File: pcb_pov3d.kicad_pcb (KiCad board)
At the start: 4 copper layers, 98 x 90 mm, 95 parts, among them P1 CONN_4X2, P2 CONN_6, P3 MICRO-SD, P4 CONN_2, P5 KNUSB, P6 CONN_12, U1 TLC5955, U2 TLC5955, U3 TLC5955, U4 STM32F40X_LQFP64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

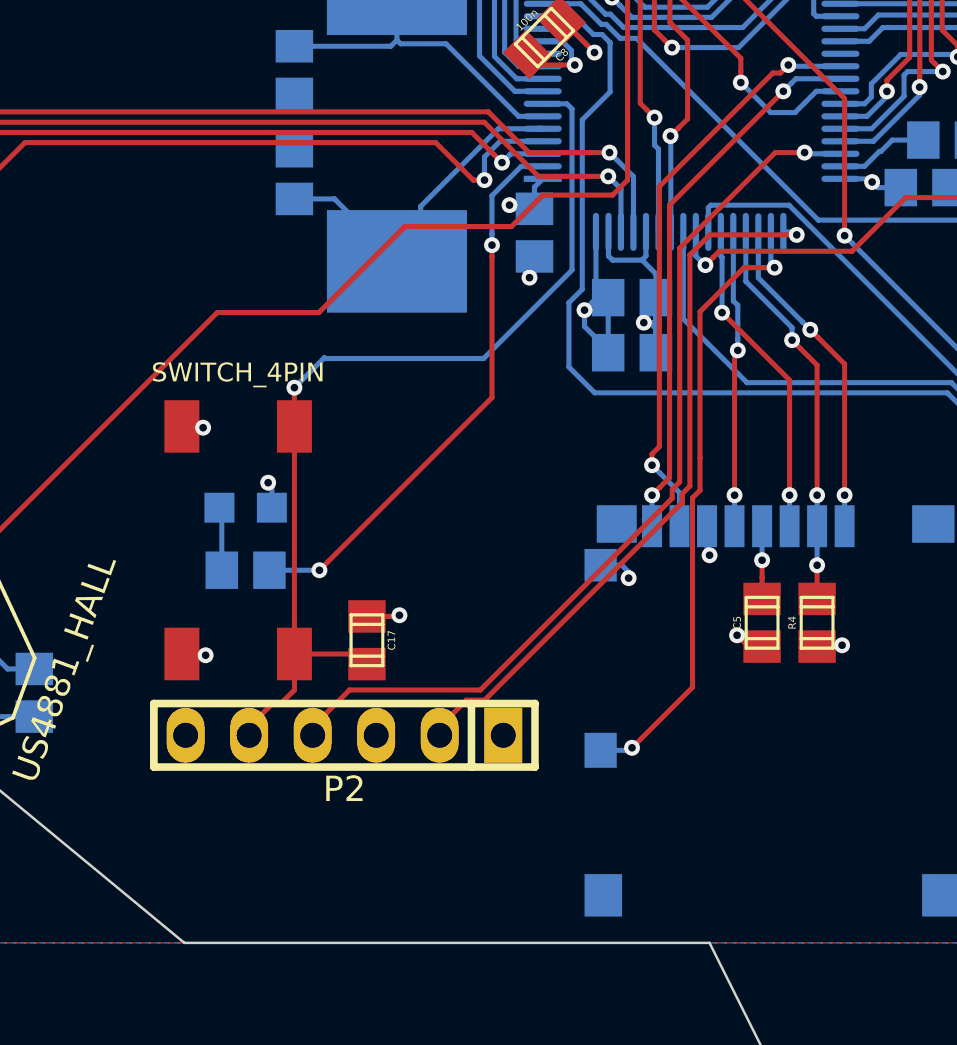
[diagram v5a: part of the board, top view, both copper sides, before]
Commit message: Move programmer connector away from rim of spindle_mount
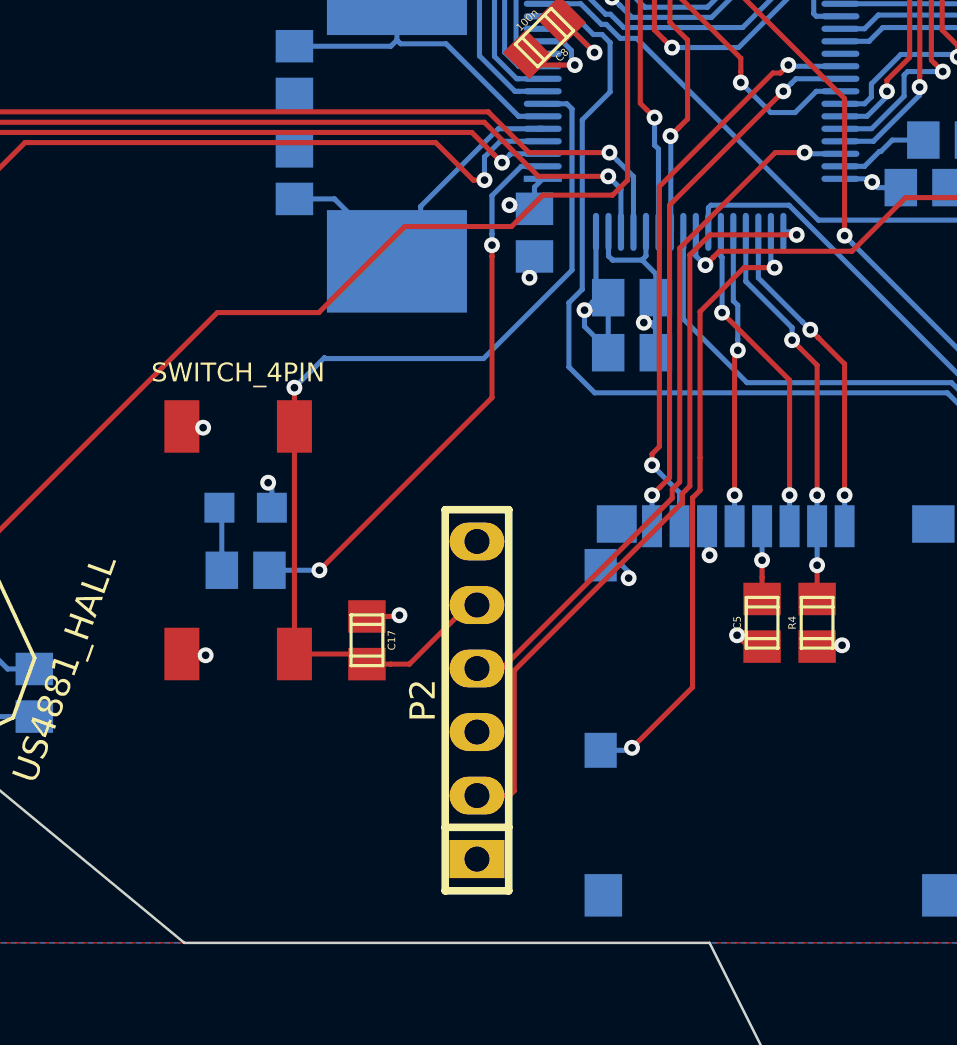
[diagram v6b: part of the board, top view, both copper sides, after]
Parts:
- moved P2 5.48 mm to (78.2, 124.8), turned to 90 degrees
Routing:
- net /swdio: track 36.7 -> 28.8 mm
- net /swclk: track 29.0 -> 31.1 mm
- net /MCU_Pwr/nrst: track 38.7 -> 40.0 mm
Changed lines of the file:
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@@
     (thickness 1.6)
     (drawings 31)
-    (tracks 2578)
+    (tracks 2576)
     (zones 0)
     (modules 95)
@@
   )
   (module w_pin_strip:pin_strip_6 (layer F.Cu)
-    (at 72.9 126.2 180)
+    (at 78.2 124.8 90)
     (descr "Pin strip 6pin")
     (tags "CONN DEV")
-    (fp_text reference P2 (at 0 -2.159 180) (layer F.SilkS)
+    (fp_text reference P2 (at 0 -2.159 90) (layer F.SilkS)
       (effects (font (size 1.016 1.016) (thickness 0.2032)))
     )
-    (fp_text value CONN_6 (at 0.254 -3.556 180) (layer F.SilkS) hide
+    (fp_text value CONN_6 (at 0.254 -3.556 90) (layer F.SilkS) hide
       (effects (font (size 1.016 0.889) (thickness 0.2032)))
     )
@@
     (fp_line (start 7.62 -1.27) (end 7.62 1.27) (layer F.SilkS) (width 0.3048))
     (fp_line (start 7.62 1.27) (end -7.62 1.27) (layer F.SilkS) (width 0.3048))
-    (pad 1 thru_hole rect (at -6.35 0 180) (size 1.524 2.19964) (drill 1.00076) (layers *.Cu *.Mask F.SilkS)
+    (pad 1 thru_hole rect (at -6.35 0 90) (size 1.524 2.19964) (drill 1.00076) (layers *.Cu *.Mask F.SilkS)
       (net 207 +3V3))
-    (pad 2 thru_hole oval (at -3.81 0 180) (size 1.524 2.19964) (drill 1.00076) (layers *.Cu *.Mask F.SilkS)
+    (pad 2 thru_hole oval (at -3.81 0 90) (size 1.524 2.19964) (drill 1.00076) (layers *.Cu *.Mask F.SilkS)
       (net 161 /swclk))
-    (pad 3 thru_hole oval (at -1.27 0 180) (size 1.524 2.19964) (drill 1.00076) (layers *.Cu *.Mask F.SilkS)
+    (pad 3 thru_hole oval (at -1.27 0 90) (size 1.524 2.19964) (drill 1.00076) (layers *.Cu *.Mask F.SilkS)
       (net 2 GND))
-    (pad 4 thru_hole oval (at 1.27 0 180) (size 1.524 2.19964) (drill 1.00076) (layers *.Cu *.Mask F.SilkS)
+    (pad 4 thru_hole oval (at 1.27 0 90) (size 1.524 2.19964) (drill 1.00076) (layers *.Cu *.Mask F.SilkS)
       (net 162 /swdio))
-    (pad 5 thru_hole oval (at 3.81 0 180) (size 1.524 2.19964) (drill 1.00076) (layers *.Cu *.Mask F.SilkS)
+    (pad 5 thru_hole oval (at 3.81 0 90) (size 1.524 2.19964) (drill 1.00076) (layers *.Cu *.Mask F.SilkS)
       (net 1 /MCU_Pwr/nrst))
-    (pad 6 thru_hole oval (at 6.35 0 180) (size 1.524 2.19964) (drill 1.00076) (layers *.Cu *.Mask F.SilkS)
+    (pad 6 thru_hole oval (at 6.35 0 90) (size 1.524 2.19964) (drill 1.00076) (layers *.Cu *.Mask F.SilkS)
       (net 163 "Net-(P2-Pad6)"))
     (model walter/pin_strip/pin_strip_6.wrl
@@
   (gr_line (start 149 94.5) (end 148 84) (angle 90) (layer Edge.Cuts) (width 0.1))
   (gr_circle (center 100 100) (end 101.5 100) (layer F.SilkS) (width 0.2))
-  (segment (start 70.90044 122.94914) (end 70.90044 124.38956) (width 0.2032) (layer F.Cu) (net 1))
-  (segment (start 70.90044 124.38956) (end 70.39302 124.89698) (width 0.2032) (layer F.Cu) (net 1))
-  (segment (start 70.39302 124.89698) (end 70.0552 124.89698) (width 0.2032) (layer F.Cu) (net 1))
-  (segment (start 70.0552 124.89698) (end 69.09 125.86218) (width 0.2032) (layer F.Cu) (net 1))
-  (segment (start 69.09 125.86218) (end 69.09 126.2) (width 0.2032) (layer F.Cu) (net 1))
+  (segment (start 78.2 120.99) (end 77.86218 120.99) (width 0.2032) (layer F.Cu) (net 1))
+  (segment (start 77.86218 120.99) (end 75.49968 123.3525) (width 0.2032) (layer F.Cu) (net 1))
+  (segment (start 75.49968 123.3525) (end 74.7525 123.3525) (width 0.2032) (layer F.Cu) (net 1))
+  (segment (start 74.7525 123.3525) (end 73.8 123.3525) (width 0.2032) (layer F.Cu) (net 1))
+  (segment (start 73.9 123.4) (end 73.8 123.3525) (width 0.2032) (layer F.Cu) (net 1))
   (segment (start 70.90044 122.94914) (end 73.39664 122.94914) (width 0.2032) (layer F.Cu) (net 1))
   (segment (start 73.39664 122.94914) (end 73.8 123.3525) (width 0.2032) (layer F.Cu) (net 1))
@@
   (segment (start 82.098224 89.48077) (end 79.76325 91.815744) (width 0.2032) (layer B.Cu) (net 160))
   (segment (start 89.20749 80.39) (end 91.75 82.93251) (width 0.2032) (layer B.Cu) (net 160))
+  (segment (start 86.362566 116.937434) (end 79.68916 123.61084) (width 0.2032) (layer F.Cu) (net 161))
+  (segment (start 78.2 128.61) (end 79.50302 128.61) (width 0.2032) (layer F.Cu) (net 161))
+  (segment (start 79.50302 128.61) (end 79.68916 128.42386) (width 0.2032) (layer F.Cu) (net 161))
+  (segment (start 79.68916 128.42386) (end 79.68916 123.61084) (width 0.2032) (layer F.Cu) (net 161))
   (segment (start 86.41282 116.53668) (end 86.41282 116.937434) (width 0.2032) (layer F.Cu) (net 161))
-  (segment (start 77.776801 124.795379) (end 76.71 125.86218) (width 0.2032) (layer F.Cu) (net 161))
   (segment (start 87.509628 106.190372) (end 86.712818 106.987182) (width 0.2032) (layer F.Cu) (net 161))
   (segment (start 86.41282 116.937434) (end 86.362566 116.937434) (width 0.2032) (layer F.Cu) (net 161))
   (segment (start 86.712818 106.987182) (end 86.712818 116.236682) (width 0.2032) (layer F.Cu) (net 161))
-  (segment (start 76.71 125.86218) (end 76.71 126.2) (width 0.2032) (layer F.Cu) (net 161))
   (segment (start 90.985528 106.190372) (end 87.509628 106.190372) (width 0.2032) (layer F.Cu) (net 161))
   (segment (start 86.712818 116.236682) (end 86.41282 116.53668) (width 0.2032) (layer F.Cu) (net 161))
-  (segment (start 86.362566 116.937434) (end 78.504621 124.795379) (width 0.2032) (layer F.Cu) (net 161))
-  (segment (start 78.504621 124.795379) (end 77.776801 124.795379) (width 0.2032) (layer F.Cu) (net 161))
   (via (at 90.985528 106.190372) (size 0.635) (drill 0.3048) (layers F.Cu B.Cu) (net 161))
   (segment (start 90.865096 106.06994) (end 90.985528 106.190372) (width 0.2032) (layer B.Cu) (net 161))
   (segment (start 90.45158 106.06994) (end 90.865096 106.06994) (width 0.2032) (layer B.Cu) (net 161))
-  (segment (start 90.12525 102.9) (end 86.306408 106.718842) (width 0.2032) (layer F.Cu) (net 162))
-  (segment (start 91.3 102.9) (end 90.12525 102.9) (width 0.2032) (layer F.Cu) (net 162))
-  (segment (start 86.306408 116.068342) (end 86.00641 116.36834) (width 0.2032) (layer F.Cu) (net 162))
-  (segment (start 86.00641 116.71884) (end 78.336281 124.388969) (width 0.2032) (layer F.Cu) (net 162))
-  (segment (start 71.63 125.86218) (end 71.63 126.2) (width 0.2032) (layer F.Cu) (net 162))
-  (segment (start 73.103211 124.388969) (end 71.63 125.86218) (width 0.2032) (layer F.Cu) (net 162))
-  (segment (start 78.336281 124.388969) (end 73.103211 124.388969) (width 0.2032) (layer F.Cu) (net 162))
-  (segment (start 86.00641 116.36834) (end 86.00641 116.71884) (width 0.2032) (layer F.Cu) (net 162))
-  (segment (start 86.306408 106.718842) (end 86.306408 116.068342) (width 0.2032) (layer F.Cu) (net 162))
+  (segment (start 78.2 123.53) (end 79.19525 123.53) (width 0.2032) (layer F.Cu) (net 162))
+  (segment (start 79.19525 123.53) (end 86.00641 116.71884) (width 0.2032) (layer F.Cu) (net 162))
+  (segment (start 86.00641 116.71884) (end 86.00641 116.36834) (width 0.2032) (layer F.Cu) (net 162))
+  (segment (start 86.00641 116.36834) (end 86.306408 116.068342) (width 0.2032) (layer F.Cu) (net 162))
+  (segment (start 86.306408 116.068342) (end 86.306408 106.718842) (width 0.2032) (layer F.Cu) (net 162))
+  (segment (start 86.306408 106.718842) (end 90.12525 102.9) (width 0.2032) (layer F.Cu) (net 162))
+  (segment (start 90.12525 102.9) (end 91.3 102.9) (width 0.2032) (layer F.Cu) (net 162))
   (segment (start 91.34828 102.94828) (end 91.3 102.9) (width 0.2032) (layer B.Cu) (net 162))
   (segment (start 92.7325 102.94828) (end 91.34828 102.94828) (width 0.2032) (layer B.Cu) (net 162))
